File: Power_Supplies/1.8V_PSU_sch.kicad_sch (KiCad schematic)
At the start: 11 parts, among them U12 TPS73601DBV, U2 TPS62822DLC

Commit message: big things are coming...
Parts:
- renumbered C1 to C3, R30 to R6, R31 to R7, R3 to R8, R4 to R9, Rpg1 to Rpg2, U2 to U3, U12 to U4
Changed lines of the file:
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@@
 		(dnp no)
 		(fields_autoplaced yes)
-		(property "Reference" "#PWR02"
+		(property "Reference" "#PWR08"
 			(at 130.81 81.28 0)
 			(effects
@@
 			(project "Power_Supplies"
 				(path "/5266cf9e-da90-4c53-80fd-cf3dbed42632/9c32f96f-6431-432f-ba4b-d32b848998a9"
-					(reference "#PWR02")
+					(reference "#PWR08")
 					(unit 1)
 				)
@@
 		(dnp no)
 		(fields_autoplaced yes)
-		(property "Reference" "#PWR06"
+		(property "Reference" "#PWR011"
 			(at 171.45 87.63 0)
 			(effects
@@
 			(project "Power_Supplies"
 				(path "/5266cf9e-da90-4c53-80fd-cf3dbed42632/9c32f96f-6431-432f-ba4b-d32b848998a9"
-					(reference "#PWR06")
+					(reference "#PWR011")
 					(unit 1)
 				)
@@
 		(dnp no)
 		(fields_autoplaced yes)
-		(property "Reference" "U12"
+		(property "Reference" "U4"
 			(at 142.24 109.22 0)
 			(effects
@@
 			(project "Power_Supplies"
 				(path "/5266cf9e-da90-4c53-80fd-cf3dbed42632/9c32f96f-6431-432f-ba4b-d32b848998a9"
-					(reference "U12")
+					(reference "U4")
 					(unit 1)
 				)
@@
 		(dnp no)
 		(fields_autoplaced yes)
-		(property "Reference" "#PWR057"
+		(property "Reference" "#PWR010"
 			(at 161.29 138.43 0)
 			(effects
@@
 			(project "Power_Supplies"
 				(path "/5266cf9e-da90-4c53-80fd-cf3dbed42632/9c32f96f-6431-432f-ba4b-d32b848998a9"
-					(reference "#PWR057")
+					(reference "#PWR010")
 					(unit 1)
 				)
@@
 		(dnp no)
 		(fields_autoplaced yes)
-		(property "Reference" "R4"
+		(property "Reference" "R9"
 			(at 173.99 71.1199 0)
 			(effects
@@
 			(project "Power_Supplies"
 				(path "/5266cf9e-da90-4c53-80fd-cf3dbed42632/9c32f96f-6431-432f-ba4b-d32b848998a9"
-					(reference "R4")
+					(reference "R9")
 					(unit 1)
 				)
@@
 		(dnp no)
 		(fields_autoplaced yes)
-		(property "Reference" "U2"
+		(property "Reference" "U3"
 			(at 130.81 46.99 0)
 			(effects
@@
 			(project "Power_Supplies"
 				(path "/5266cf9e-da90-4c53-80fd-cf3dbed42632/9c32f96f-6431-432f-ba4b-d32b848998a9"
-					(reference "U2")
+					(reference "U3")
 					(unit 1)
 				)
@@
 		(dnp no)
 		(fields_autoplaced yes)
-		(property "Reference" "R30"
+		(property "Reference" "R6"
 			(at 163.83 119.3799 0)
 			(effects
@@
 			(project "Power_Supplies"
 				(path "/5266cf9e-da90-4c53-80fd-cf3dbed42632/9c32f96f-6431-432f-ba4b-d32b848998a9"
-					(reference "R30")
+					(reference "R6")
 					(unit 1)
 				)
@@
 		(dnp no)
 		(fields_autoplaced yes)
-		(property "Reference" "#PWR01"
+		(property "Reference" "#PWR07"
 			(at 113.03 81.28 0)
 			(effects
@@
 			(project "Power_Supplies"
 				(path "/5266cf9e-da90-4c53-80fd-cf3dbed42632/9c32f96f-6431-432f-ba4b-d32b848998a9"
-					(reference "#PWR01")
+					(reference "#PWR07")
 					(unit 1)
 				)
@@
 		(dnp no)
 		(fields_autoplaced yes)
-		(property "Reference" "#PWR07"
+		(property "Reference" "#PWR012"
 			(at 186.69 83.82 0)
 			(effects
@@
 			(project "Power_Supplies"
 				(path "/5266cf9e-da90-4c53-80fd-cf3dbed42632/9c32f96f-6431-432f-ba4b-d32b848998a9"
-					(reference "#PWR07")
+					(reference "#PWR012")
 					(unit 1)
 				)
@@
 		(dnp no)
 		(fields_autoplaced yes)
-		(property "Reference" "R31"
+		(property "Reference" "R7"
 			(at 163.83 126.9999 0)
 			(effects
@@
 			(project "Power_Supplies"
 				(path "/5266cf9e-da90-4c53-80fd-cf3dbed42632/9c32f96f-6431-432f-ba4b-d32b848998a9"
-					(reference "R31")
+					(reference "R7")
 					(unit 1)
 				)
@@
 		(dnp no)
 		(fields_autoplaced yes)
-		(property "Reference" "Rpg1"
+		(property "Reference" "Rpg2"
 			(at 118.11 59.6899 0)
 			(effects
@@
 			(project "Power_Supplies"
 				(path "/5266cf9e-da90-4c53-80fd-cf3dbed42632/9c32f96f-6431-432f-ba4b-d32b848998a9"
-					(reference "Rpg1")
+					(reference "Rpg2")
 					(unit 1)
 				)
@@
 		(dnp no)
 		(fields_autoplaced yes)
-		(property "Reference" "C1"
+		(property "Reference" "C3"
 			(at 116.84 68.5799 0)
 			(effects
@@
 			(project "Power_Supplies"
 				(path "/5266cf9e-da90-4c53-80fd-cf3dbed42632/9c32f96f-6431-432f-ba4b-d32b848998a9"
-					(reference "C1")
+					(reference "C3")
 					(unit 1)
 				)
@@
 		(dnp no)
 		(fields_autoplaced yes)
-		(property "Reference" "R3"
+		(property "Reference" "R8"
 			(at 173.99 58.4199 0)
 			(effects
@@
 			(project "Power_Supplies"
 				(path "/5266cf9e-da90-4c53-80fd-cf3dbed42632/9c32f96f-6431-432f-ba4b-d32b848998a9"
-					(reference "R3")
+					(reference "R8")
 					(unit 1)
 				)
@@
 		(dnp no)
 		(fields_autoplaced yes)
-		(property "Reference" "#PWR058"
+		(property "Reference" "#PWR09"
 			(at 142.24 133.35 0)
 			(effects
@@
 			(project "Power_Supplies"
 				(path "/5266cf9e-da90-4c53-80fd-cf3dbed42632/9c32f96f-6431-432f-ba4b-d32b848998a9"
-					(reference "#PWR058")
-					(unit 1)
-				)
+					(reference "#PWR09")
+					(unit 1)
+				)

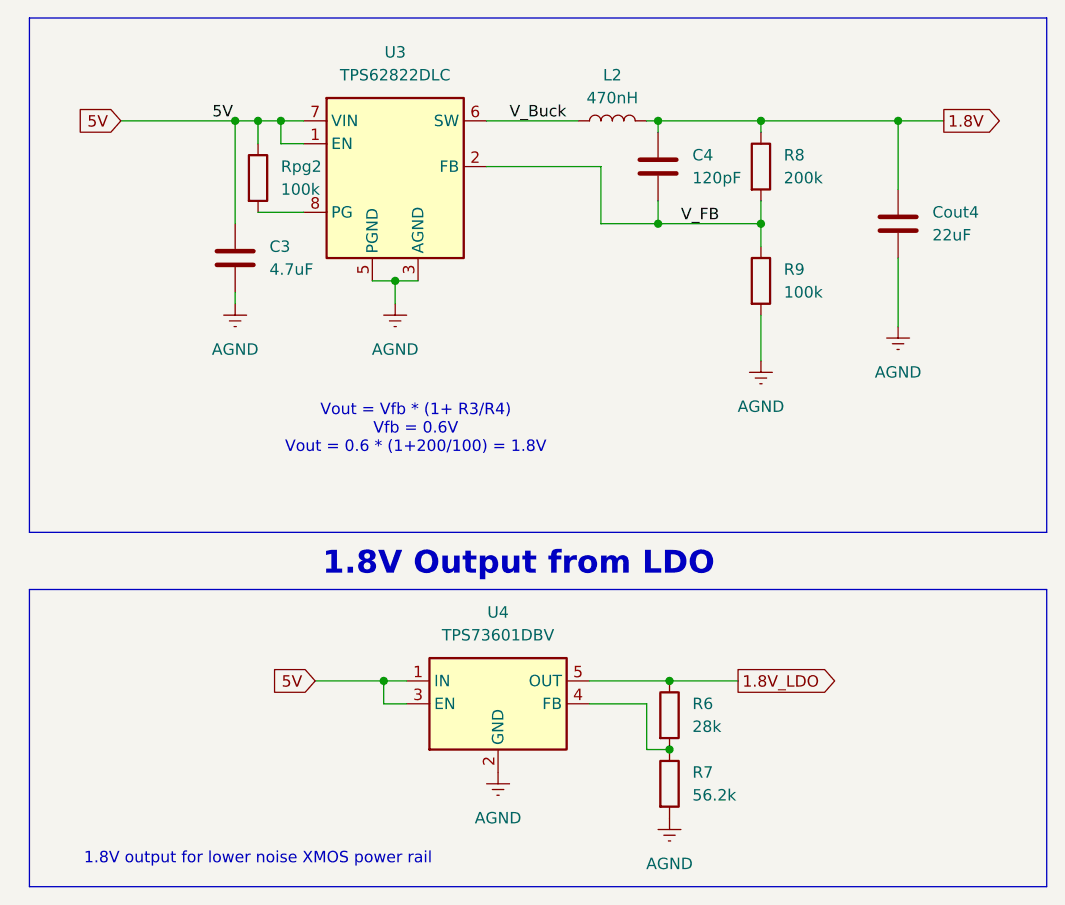
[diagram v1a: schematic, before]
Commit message: Added stuff for the power supply circuitry
changed all grounds to GND (same ground plane)
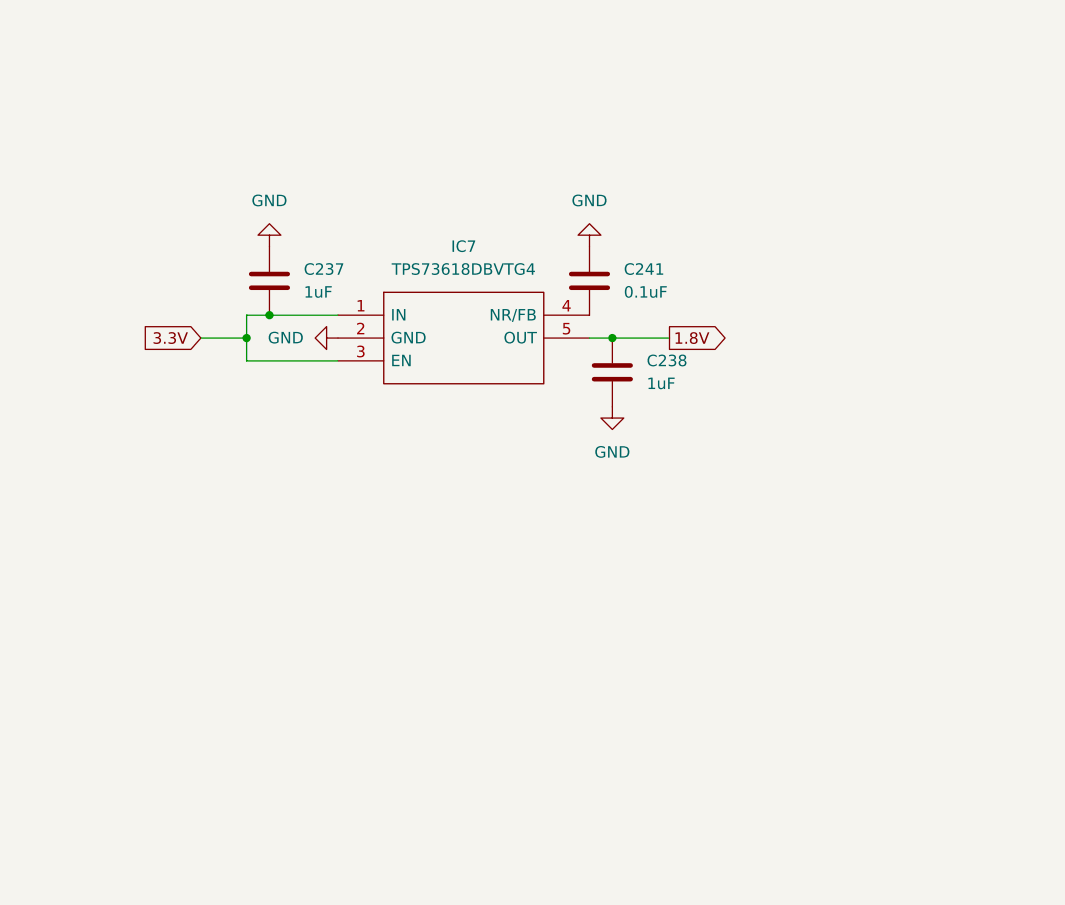
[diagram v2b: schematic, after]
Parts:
- removed C3: 4.7uF, Capacitor_SMD:C_0805_2012Metric, symbol Device:C
- removed C4: 120pF, Capacitor_SMD:C_0402_1005Metric, symbol Device:C
- removed Cout4: 22uF, Capacitor_SMD:C_0805_2012Metric, symbol Device:C
- removed L2: 470nH, Inductor_SMD:L_0805_2012Metric, symbol Device:L
- removed R6: 28k, Resistor_SMD:R_0805_2012Metric, symbol Device:R
- removed R7: 56.2k, Resistor_SMD:R_0805_2012Metric, symbol Device:R
- removed R8: 200k, Resistor_SMD:R_0805_2012Metric, symbol Device:R
- removed R9, Rpg2: 100k, Resistor_SMD:R_0805_2012Metric, symbol Device:R
- removed U3: TPS62822DLC, Package_SON:Texas_VSON-HR-8_1.5x2mm_P0.5mm, symbol Regulator_Switching:TPS62822DLC
- removed U4: TPS73601DBV, Package_TO_SOT_SMD:SOT-23-5, symbol Regulator_Linear:TPS73601DBV
- added C237, C238: 1uF, Capacitor_SMD:C_0402_1005Metric, symbol Device:C
- added C241: 0.1uF, Capacitor_SMD:C_0402_1005Metric, symbol Device:C
- added IC7: TPS73618DBVTG4, SOT95P280X145-5N, symbol SamacSys_Parts:TPS73618DBVTG4
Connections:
- net 1.8V: now also C238.1, IC7.5 (OUT)
- new net: C241.1, IC7.4 (NR/FB)
- new net 3.3V: C237.2, IC7.1 (IN), IC7.3 (EN)
- new net GND: C237.1, C238.2, C241.2, IC7.2 (GND)
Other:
- note removed: "1.8V Output from LDO"
- note removed: "1.8V output for lower noise XMOS power rail"
- note removed: "Vout = Vfb * (1+ R3/R4) Vfb = 0.6V Vout = 0.6 * (1+200/100) = 1.8V"
